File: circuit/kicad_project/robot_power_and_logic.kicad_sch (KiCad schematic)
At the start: 20 parts

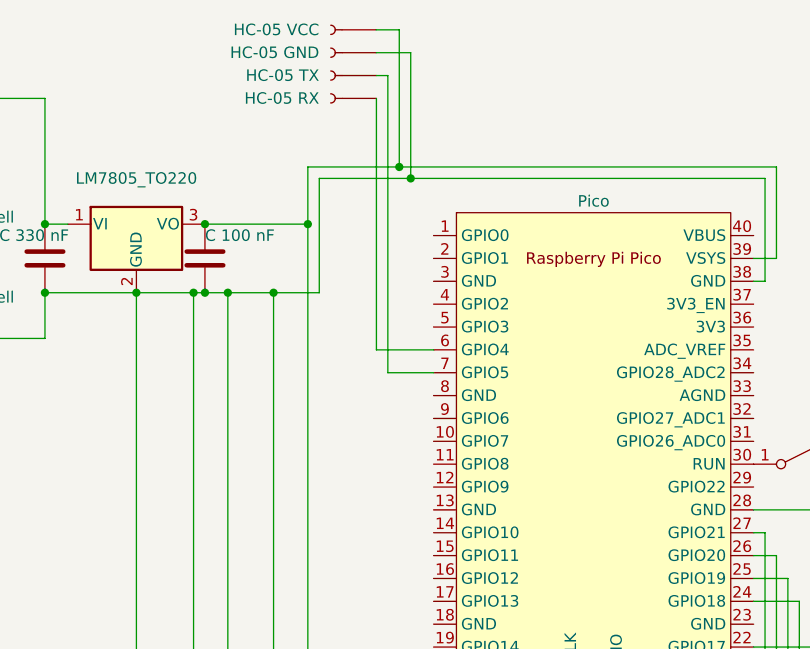
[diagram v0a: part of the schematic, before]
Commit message: Change UART pins used for communication with HC-05
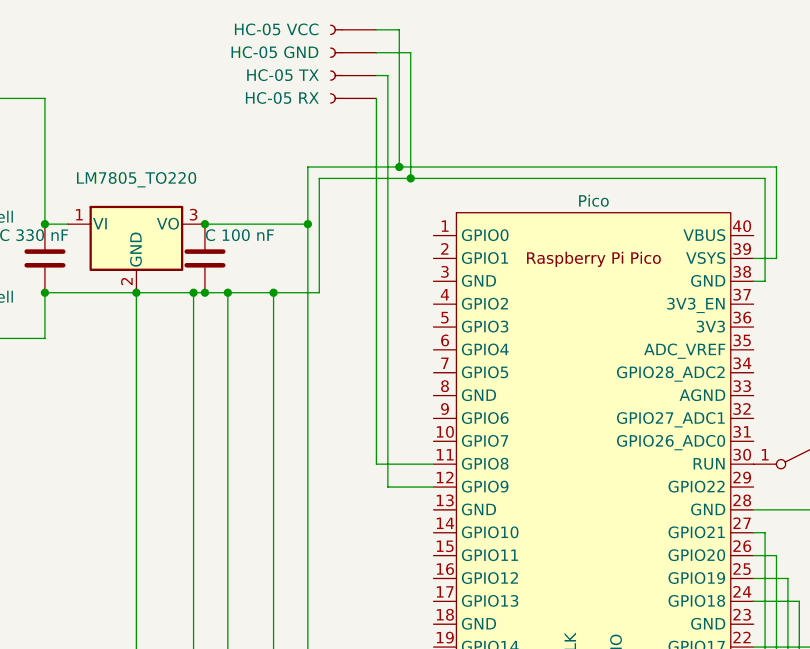
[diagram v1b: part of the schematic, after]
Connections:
- net at J?.1 (Pin_1): now also U?.11 (GPIO8); no longer U?.6 (GPIO4)
- net at U?.12 (GPIO9): now also J?.1 (Pin_1)
- net at U?.7 (GPIO5): no longer J?.1 (Pin_1)
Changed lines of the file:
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@@
+    (stroke (width 0) (type default) (color 0 0 0 0))
+  )
+  (wire (pts (xy 96.52 31.75) (xy 96.52 72.39))
     (stroke (width 0) (type default) (color 0 0 0 0))
   )
@@
     (stroke (width 0) (type default) (color 0 0 0 0))
   )
+  (wire (pts (xy 96.52 72.39) (xy 102.87 72.39))
+    (stroke (width 0) (type default) (color 0 0 0 0))
+  )
   (wire (pts (xy 43.18 31.75) (xy 39.37 31.75))
     (stroke (width 0) (type default) (color 0 0 0 0))
@@
     (stroke (width 0) (type default) (color 0 0 0 0))
   )
-  (wire (pts (xy 97.79 62.23) (xy 97.79 29.21))
+  (wire (pts (xy 97.79 74.93) (xy 97.79 29.21))
     (stroke (width 0) (type default) (color 0 0 0 0))
   )
@@
     (stroke (width 0) (type default) (color 0 0 0 0))
   )
-  (wire (pts (xy 96.52 59.69) (xy 96.52 31.75))
-    (stroke (width 0) (type default) (color 0 0 0 0))
-  )
   (wire (pts (xy 128.27 124.46) (xy 152.4 124.46))
     (stroke (width 0) (type default) (color 0 0 0 0))
@@
     (stroke (width 0) (type default) (color 0 0 0 0))
   )
-  (wire (pts (xy 102.87 62.23) (xy 97.79 62.23))
+  (wire (pts (xy 102.87 74.93) (xy 97.79 74.93))
     (stroke (width 0) (type default) (color 0 0 0 0))
   )
@@
     (stroke (width 0) (type default) (color 0 0 0 0))
   )
-  (wire (pts (xy 102.87 59.69) (xy 96.52 59.69))
-    (stroke (width 0) (type default) (color 0 0 0 0))
-  )

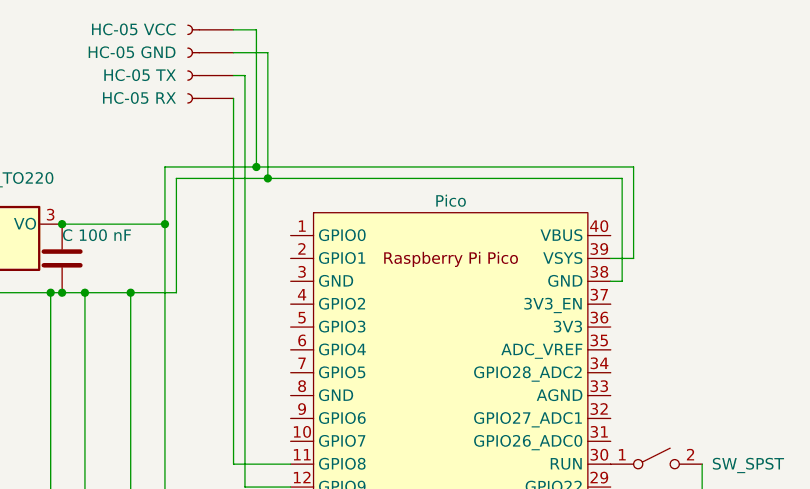
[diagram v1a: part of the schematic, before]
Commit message: Change HC-05 power source to Pico's 3V3 pin
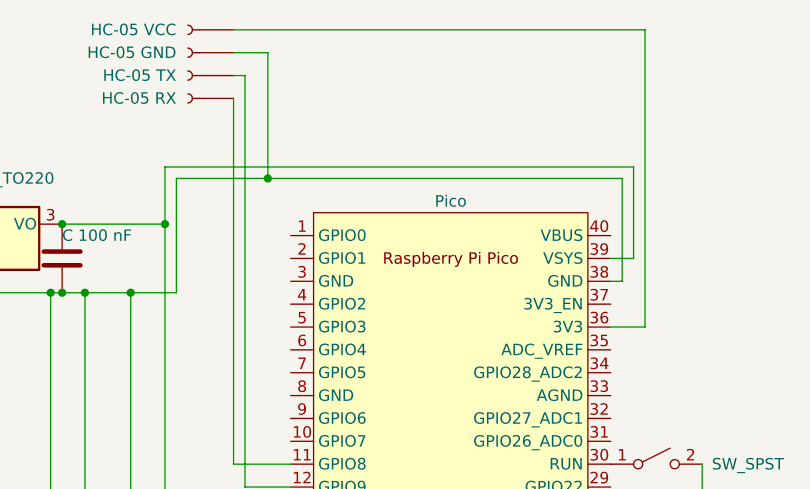
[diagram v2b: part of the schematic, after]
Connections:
- net at C?.1, C?.2, C?.2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: no longer J?.1 (Pin_1)
- net at U?.36 (3V3): now also J?.1 (Pin_1)
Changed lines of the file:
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@@
   (junction (at 110.49 156.21) (diameter 0) (color 0 0 0 0)
   )
-  (junction (at 99.06 39.37) (diameter 0) (color 0 0 0 0)
-  )
   (junction (at 76.2 167.64) (diameter 0) (color 0 0 0 0)
   )
@@
     (stroke (width 0) (type default) (color 0 0 0 0))
   )
-  (wire (pts (xy 96.52 24.13) (xy 99.06 24.13))
-    (stroke (width 0) (type default) (color 0 0 0 0))
-  )
   (wire (pts (xy 69.85 156.21) (xy 69.85 53.34))
     (stroke (width 0) (type default) (color 0 0 0 0))
@@
     (stroke (width 0) (type default) (color 0 0 0 0))
   )
+  (wire (pts (xy 142.24 24.13) (xy 142.24 57.15))
+    (stroke (width 0) (type default) (color 0 0 0 0))
+  )
   (wire (pts (xy 100.33 218.44) (xy 146.05 218.44))
     (stroke (width 0) (type default) (color 0 0 0 0))
@@
     (stroke (width 0) (type default) (color 0 0 0 0))
   )
+  (wire (pts (xy 142.24 57.15) (xy 138.43 57.15))
+    (stroke (width 0) (type default) (color 0 0 0 0))
+  )
   (wire (pts (xy 76.2 53.34) (xy 76.2 160.02))
     (stroke (width 0) (type default) (color 0 0 0 0))
@@
     (stroke (width 0) (type default) (color 0 0 0 0))
   )
+  (wire (pts (xy 96.52 24.13) (xy 142.24 24.13))
+    (stroke (width 0) (type default) (color 0 0 0 0))
+  )
   (wire (pts (xy 138.43 49.53) (xy 140.97 49.53))
     (stroke (width 0) (type default) (color 0 0 0 0))
@@
     (stroke (width 0) (type default) (color 0 0 0 0))
   )
-  (wire (pts (xy 99.06 39.37) (xy 88.9 39.37))
+  (wire (pts (xy 88.9 39.37) (xy 140.97 39.37))
     (stroke (width 0) (type default) (color 0 0 0 0))
   )
@@
     (stroke (width 0) (type default) (color 0 0 0 0))
   )
-  (wire (pts (xy 99.06 24.13) (xy 99.06 39.37))
-    (stroke (width 0) (type default) (color 0 0 0 0))
-  )
-  (wire (pts (xy 140.97 39.37) (xy 99.06 39.37))
-    (stroke (width 0) (type default) (color 0 0 0 0))
-  )
